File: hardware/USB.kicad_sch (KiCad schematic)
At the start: 33 parts, among them J10 Battery, P4 USB_C_Plug_USB2.0, Q1 DMG3415U-7, SW1 ON, U2 TP4056, U4 MT3608, U5 AP2114H-3.3

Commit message: feat(Hw):Update_Schematic_And_BOM
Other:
- moved on the sheet: C54, F1, P4, R13, R14, R15, R19

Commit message: feat(Hw):Update_Schematic
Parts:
- R44: value 10.7K -> 12.3K; LCSC# C2998172 -> C346621
- R45: value 10K -> 9.09K; LCSC# C2759535 -> C852966
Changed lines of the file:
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@@
 			)
 		)
-		(property "Value" "10K"
+		(property "Value" "9.09K"
 			(at 209.55 71.1199 0)
 			(effects
@@
 			)
 		)
-		(property "LCSC#" "C2759535"
+		(property "LCSC#" "C852966"
 			(at 207.01 69.85 0)
 			(effects
@@
 			)
 		)
-		(property "Value" "10.7K"
+		(property "Value" "12.3K"
 			(at 209.55 58.4199 0)
 			(effects
@@
 			)
 		)
-		(property "LCSC#" "C2998172"
+		(property "LCSC#" "C346621"
 			(at 207.01 57.15 0)
 			(effects

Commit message: feat(Hw):Update_Schematic_And_BOM
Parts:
- D16, D8: LCSC# C375573 -> C22371297
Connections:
- net 2_DN renamed D-
- net 2_DP renamed D+
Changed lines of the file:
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@@
 	(wire
 		(pts
-			(xy 46.99 43.18) (xy 44.45 43.18)
+			(xy 45.72 43.18) (xy 44.45 43.18)
 		)
 		(stroke
@@
 	(wire
 		(pts
-			(xy 46.99 48.26) (xy 44.45 48.26)
+			(xy 45.72 48.26) (xy 44.45 48.26)
 		)
 		(stroke
@@
 		)
 	)
-	(label "2_DP"
-		(at 46.99 48.26 0)
-		(effects
-			(font
-				(size 1.27 1.27)
-			)
-			(justify left bottom)
-		)
-	)
-	(label "2_DN"
-		(at 46.99 43.18 0)
+	(label "SW"
+		(at 177.8 118.11 0)
 		(effects
 			(font
@@
 		)
 	)
-	(label "SW"
-		(at 177.8 118.11 0)
+	(hierarchical_label "USB_DET"
+		(shape output)
+		(at 102.87 45.72 0)
 		(effects
 			(font
 				(size 1.27 1.27)
 			)
-			(justify left bottom)
+			(justify left)
 		)
 	)
-	(hierarchical_label "USB_DET"
-		(shape output)
-		(at 102.87 45.72 0)
+	(hierarchical_label "D-"
+		(shape bidirectional)
+		(at 45.72 43.18 0)
 		(effects
 			(font
@@
 		)
 	)
+	(hierarchical_label "D+"
+		(shape bidirectional)
+		(at 45.72 48.26 0)
+		(effects
+			(font
+				(size 1.27 1.27)
+			)
+			(justify left)
+		)
+	)
 	(hierarchical_label "VCC"
 		(shape output)
@@
 			)
 		)
-		(property "LCSC#" "C375573"
+		(property "LCSC#" "C22371297"
 			(at 144.78 66.04 90)
 			(effects
@@
 			)
 		)
-		(property "LCSC#" "C375573"
+		(property "LCSC#" "C22371297"
 			(at 151.13 68.58 90)
 			(effects

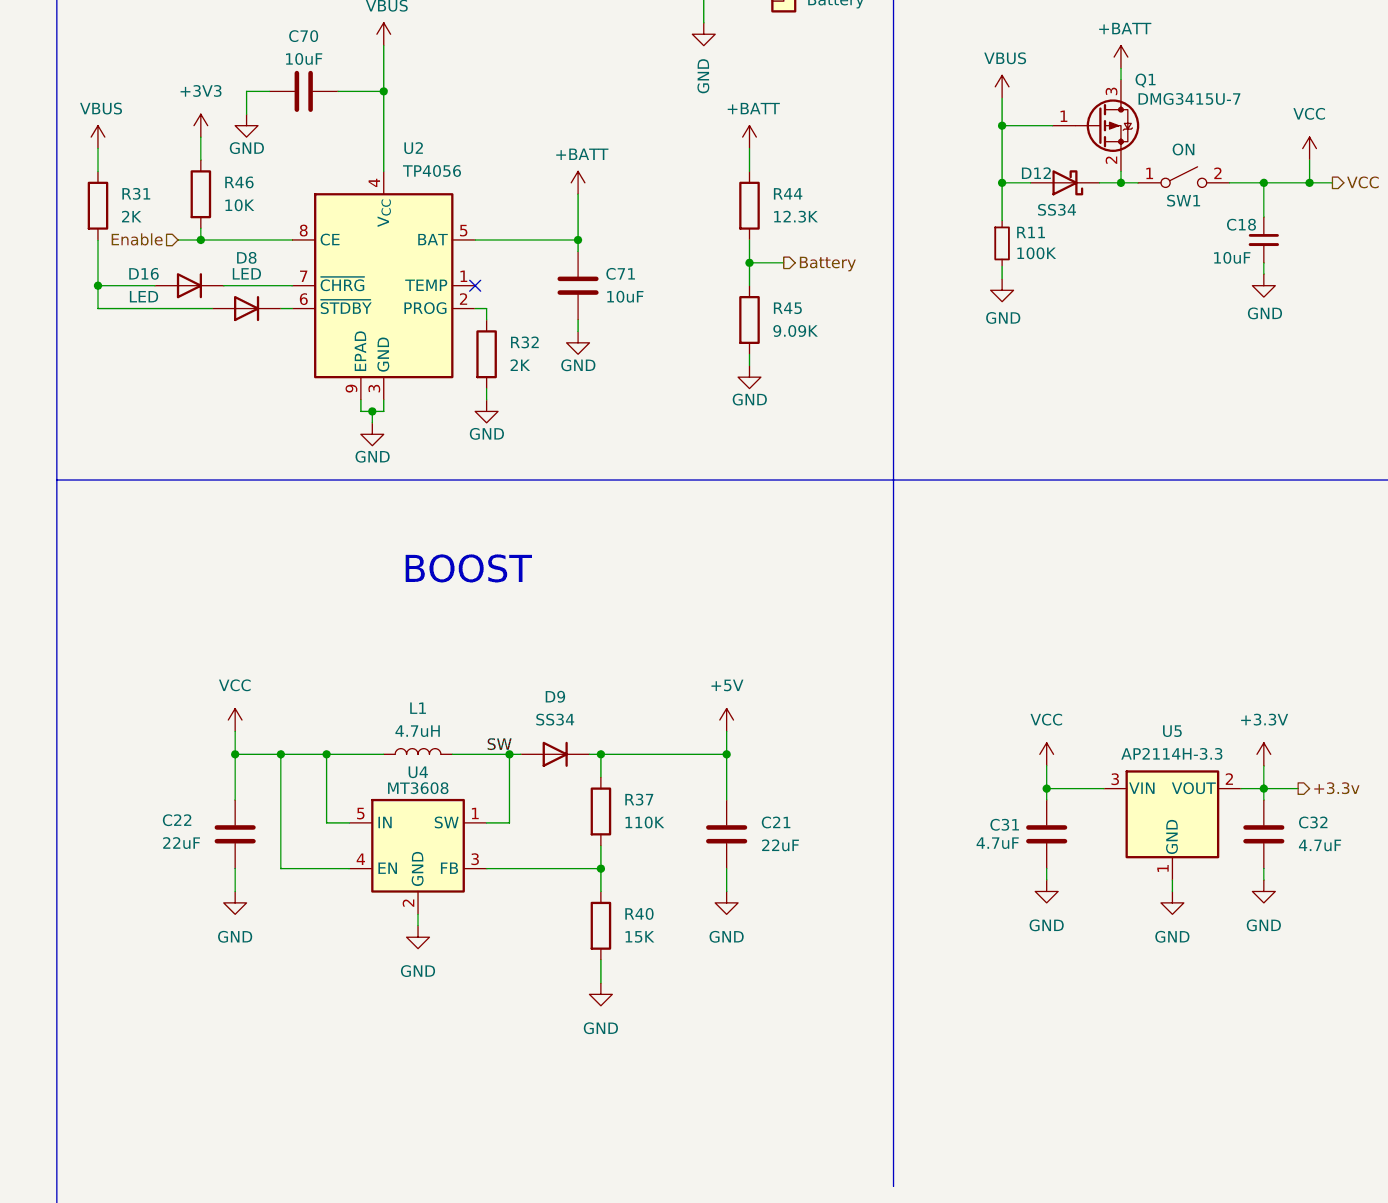
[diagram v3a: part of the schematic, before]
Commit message: feat(Hw):Update_Schematic_And_Floorplan
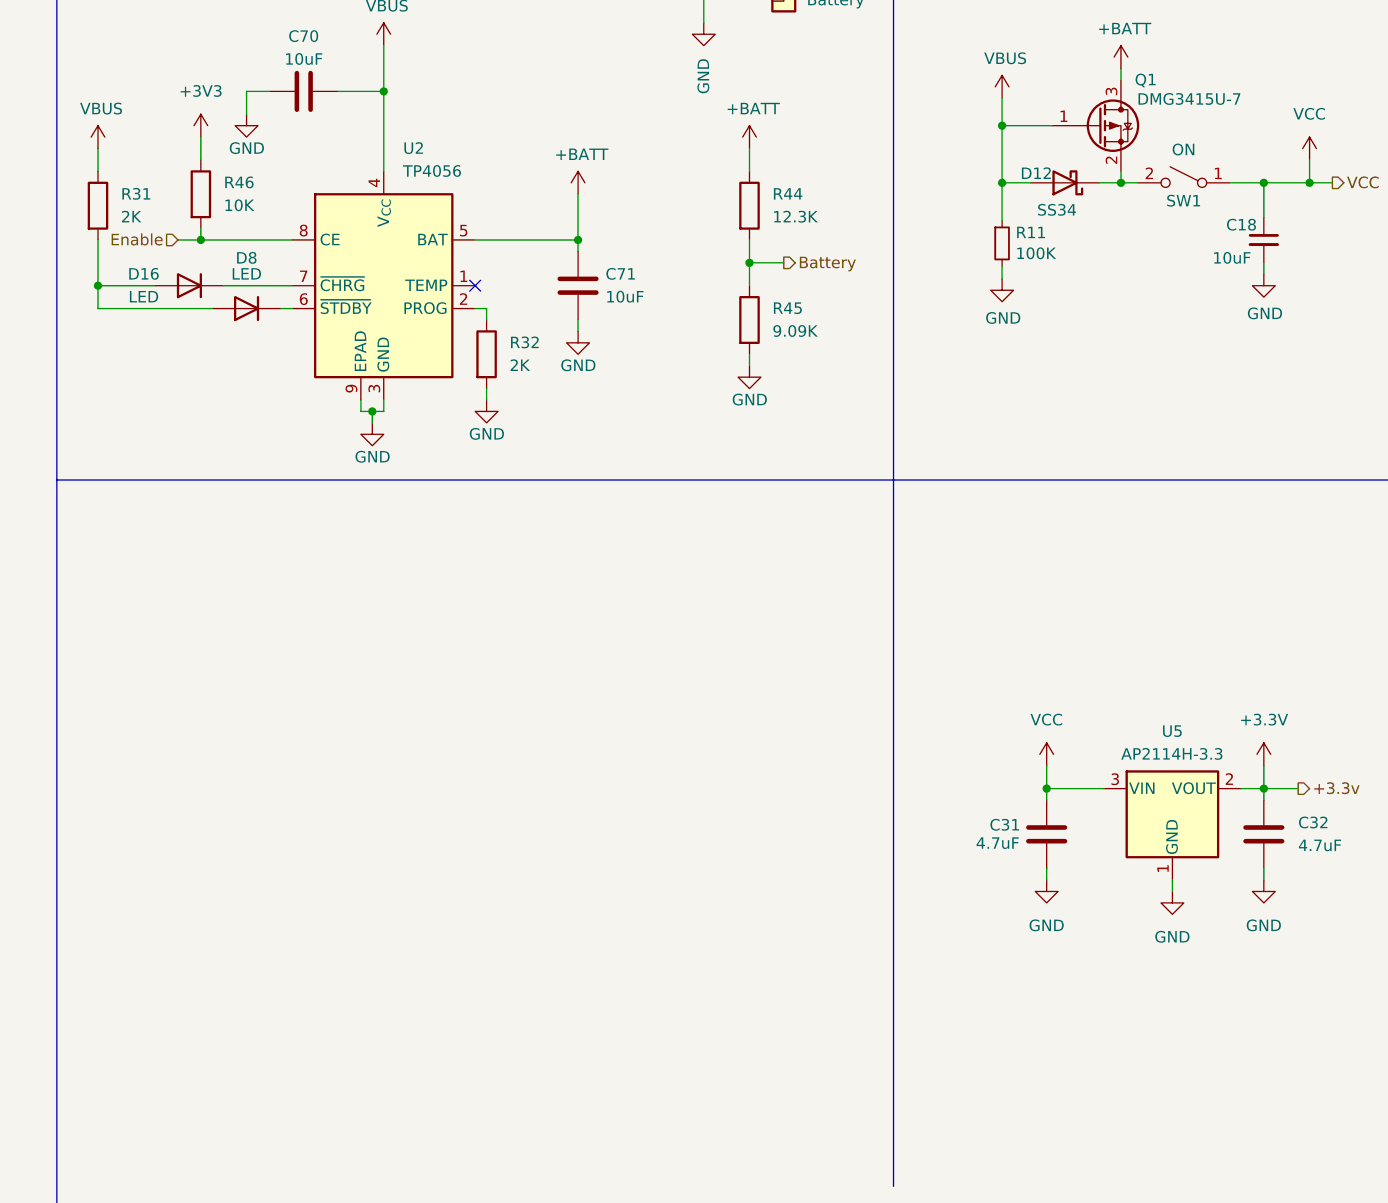
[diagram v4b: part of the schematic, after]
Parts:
- removed C21, C22: 22uF, Capacitor_SMD:C_0402_1005Metric, symbol Device:C
- removed D9: SS34, Diode_SMD:D_SMA, symbol Device:D
- removed L1: 4.7uH, Footprints:LQH5BPN, symbol Device:L
- removed R37: 110K, Resistor_SMD:R_0603_1608Metric, symbol Device:R
- removed R40: 15K, Resistor_SMD:R_0603_1608Metric, symbol Device:R
- removed U4: MT3608, Package_TO_SOT_SMD:SOT-23-6, symbol Regulator_Switching:MT3608
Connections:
- net VCC: now also SW1.1 (A); no longer SW1.2 (B)
- net at D12.1 (K), Q1.2 (S): now also SW1.2 (B); no longer SW1.1 (A)
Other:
- note removed: "BOOST"

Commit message: feat(Hw):Update_3Dmodels_And_Rear_Board
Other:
- company: (none) -> Electronic Cats
- title: (none) -> Badge-HackGDL-2026
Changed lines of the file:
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@@
 	(generator_version "9.0")
 	(paper "A4")
+	(title_block
+		(title "Badge-HackGDL-2026")
+		(date "2026-01-15")
+		(rev "v1.0")
+		(company "Electronic Cats")
+		(comment 1 "Lizeth Gallegos Martínez")
+	)
 	(text "VOLTAGE SELECTOR"
 		(exclude_from_sim no)

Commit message: feat(Hw):Update_BOM
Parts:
- J10: manf# Bateria 18650 3.7V 2200mAh ±5% -> (none)
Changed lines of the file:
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@@
 			)
 		)
-		(property "manf#" "Bateria 18650 3.7V 2200mAh ±5% "
+		(property "manf#" ""
 			(at 210.82 31.75 0)
 			(effects
